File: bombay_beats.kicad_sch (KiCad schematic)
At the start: 7 parts, among them SW9 SW_SPDT, U1 74HC165

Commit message: fix 0603 footprints
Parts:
- C1: footprint Capacitor_SMD:C_0201_0603Metric -> Capacitor_SMD:C_0603_1608Metric
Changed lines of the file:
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@@
 			)
 		)
-		(property "Footprint" "Capacitor_SMD:C_0201_0603Metric"
+		(property "Footprint" "Capacitor_SMD:C_0603_1608Metric"
 			(at 142.24 30.7848 0)
 			(effects

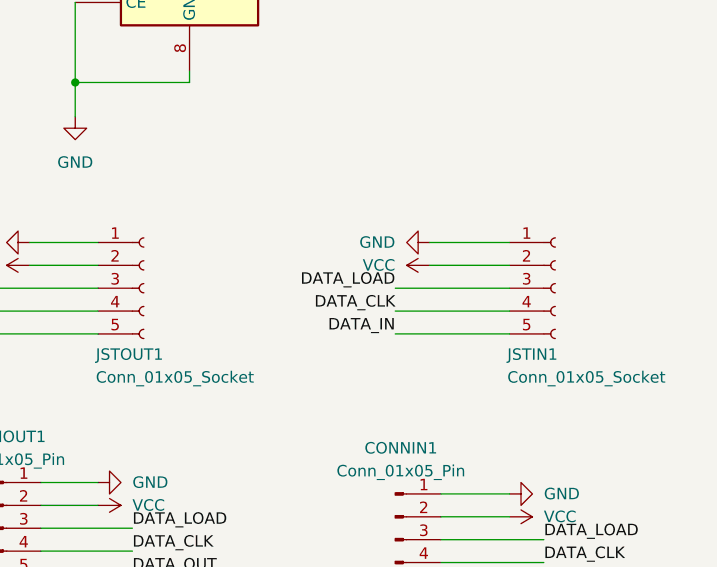
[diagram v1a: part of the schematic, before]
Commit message: fix pinout of jst input
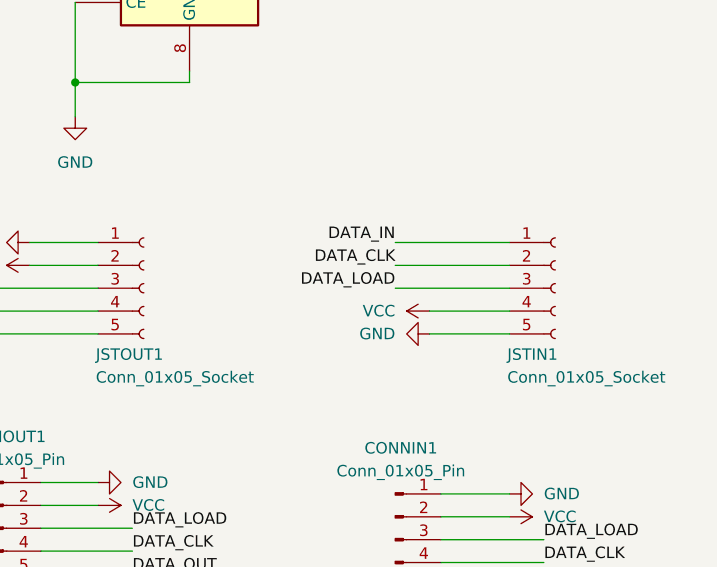
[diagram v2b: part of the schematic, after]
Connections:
- net DATA_CLK: now also JSTIN1.2 (Pin_2); no longer JSTIN1.4 (Pin_4)
- net DATA_IN: now also JSTIN1.1 (Pin_1); no longer JSTIN1.5 (Pin_5)
- net GND: now also JSTIN1.5 (Pin_5); no longer JSTIN1.1 (Pin_1)
- net VCC: now also JSTIN1.4 (Pin_4); no longer JSTIN1.2 (Pin_2)
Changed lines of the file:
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@@
-	(wire
-		(pts
-			(xy 151.13 111.76) (xy 163.83 111.76)
-		)
-		(stroke
-			(width 0)
-			(type default)
-		)
-	)
 	(wire
 		(pts
@@
 	(wire
 		(pts
+			(xy 154.94 111.76) (xy 163.83 111.76)
+		)
+		(stroke
+			(width 0)
+			(type default)
+		)
+	)
+	(wire
+		(pts
 			(xy 115.57 83.82) (xy 128.27 83.82)
 		)
@@
 	(wire
 		(pts
+			(xy 151.13 101.6) (xy 163.83 101.6)
+		)
+		(stroke
+			(width 0)
+			(type default)
+		)
+	)
+	(wire
+		(pts
 			(xy 106.68 106.68) (xy 118.11 106.68)
 		)
@@
 	(wire
 		(pts
-			(xy 154.94 101.6) (xy 163.83 101.6)
-		)
-		(stroke
-			(width 0)
-			(type default)
-		)
-	)
-	(wire
-		(pts
 			(xy 92.71 59.69) (xy 115.57 59.69)
 		)
@@
 	(wire
 		(pts
+			(xy 151.13 106.68) (xy 163.83 106.68)
+		)
+		(stroke
+			(width 0)
+			(type default)
+		)
+	)
+	(wire
+		(pts
 			(xy 109.22 20.32) (xy 118.11 20.32)
 		)
@@
 	(wire
 		(pts
+			(xy 151.13 104.14) (xy 163.83 104.14)
+		)
+		(stroke
+			(width 0)
+			(type default)
+		)
+	)
+	(wire
+		(pts
 			(xy 85.09 52.07) (xy 85.09 72.39)
 		)
@@
 	(wire
 		(pts
-			(xy 151.13 106.68) (xy 163.83 106.68)
-		)
-		(stroke
-			(width 0)
-			(type default)
-		)
-	)
-	(wire
-		(pts
 			(xy 92.71 99.06) (xy 92.71 59.69)
 		)
@@
 	(wire
 		(pts
-			(xy 154.94 104.14) (xy 163.83 104.14)
-		)
-		(stroke
-			(width 0)
-			(type default)
-		)
-	)
-	(wire
-		(pts
 			(xy 110.49 104.14) (xy 118.11 104.14)
 		)
@@
 	(wire
 		(pts
-			(xy 151.13 109.22) (xy 163.83 109.22)
+			(xy 154.94 109.22) (xy 163.83 109.22)
 		)
 		(stroke
@@
 	)
 	(label "DATA_CLK"
-		(at 151.13 109.22 180)
+		(at 151.13 104.14 180)
 		(fields_autoplaced yes)
 		(effects
@@
 	)
 	(label "DATA_IN"
-		(at 151.13 111.76 180)
+		(at 151.13 101.6 180)
 		(fields_autoplaced yes)
 		(effects
@@
 		(lib_name "GND_1")
 		(lib_id "power:GND")
-		(at 154.94 101.6 270)
+		(at 154.94 111.76 270)
 		(unit 1)
 		(exclude_from_sim no)
@@
 		(on_board yes)
 		(dnp no)
-		(fields_autoplaced yes)
 		(property "Reference" "#PWR03"
-			(at 148.59 101.6 0)
+			(at 148.59 111.76 0)
 			(effects
 				(font
@@
 		)
 		(property "Value" "GND"
-			(at 151.13 101.5999 90)
+			(at 151.13 111.7599 90)
 			(effects
 				(font
@@
 		)
 		(property "Footprint" ""
-			(at 154.94 101.6 0)
+			(at 154.94 111.76 0)
 			(effects
 				(font
@@
 		)
 		(property "Datasheet" ""
-			(at 154.94 101.6 0)
+			(at 154.94 111.76 0)
 			(effects
 				(font
@@
 		)
 		(property "Description" "Power symbol creates a global label with name \"GND\" , ground"
-			(at 154.94 101.6 0)
+			(at 154.94 111.76 0)
 			(effects
 				(font
@@
 	(symbol
 		(lib_id "power:VCC")
-		(at 154.94 104.14 90)
+		(at 154.94 109.22 90)
 		(unit 1)
 		(exclude_from_sim no)
@@
 		(fields_autoplaced yes)
 		(property "Reference" "#PWR06"
-			(at 158.75 104.14 0)
+			(at 158.75 109.22 0)
 			(effects
 				(font
@@
 		)
 		(property "Value" "VCC"
-			(at 151.13 104.1399 90)
+			(at 151.13 109.2199 90)
 			(effects
 				(font
@@
 		)
 		(property "Footprint" ""
-			(at 154.94 104.14 0)
+			(at 154.94 109.22 0)
 			(effects
 				(font
@@
 		)
 		(property "Datasheet" ""
-			(at 154.94 104.14 0)
+			(at 154.94 109.22 0)
 			(effects
 				(font
@@
 		)
 		(property "Description" "Power symbol creates a global label with name \"VCC\""
-			(at 154.94 104.14 0)
-			(effects
-				(font
+			(at 154.94 109.22 0)
+			(effects
+				(font
